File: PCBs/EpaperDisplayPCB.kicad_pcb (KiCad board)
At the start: 2 copper layers, 84 x 40.1 mm, 52 parts, among them J1 Conn_01x12_FPC_0.5mm, J2 Conn_01x08, Q1 AO3404A, U1 ePaper-2.66, U2 LIS3DH

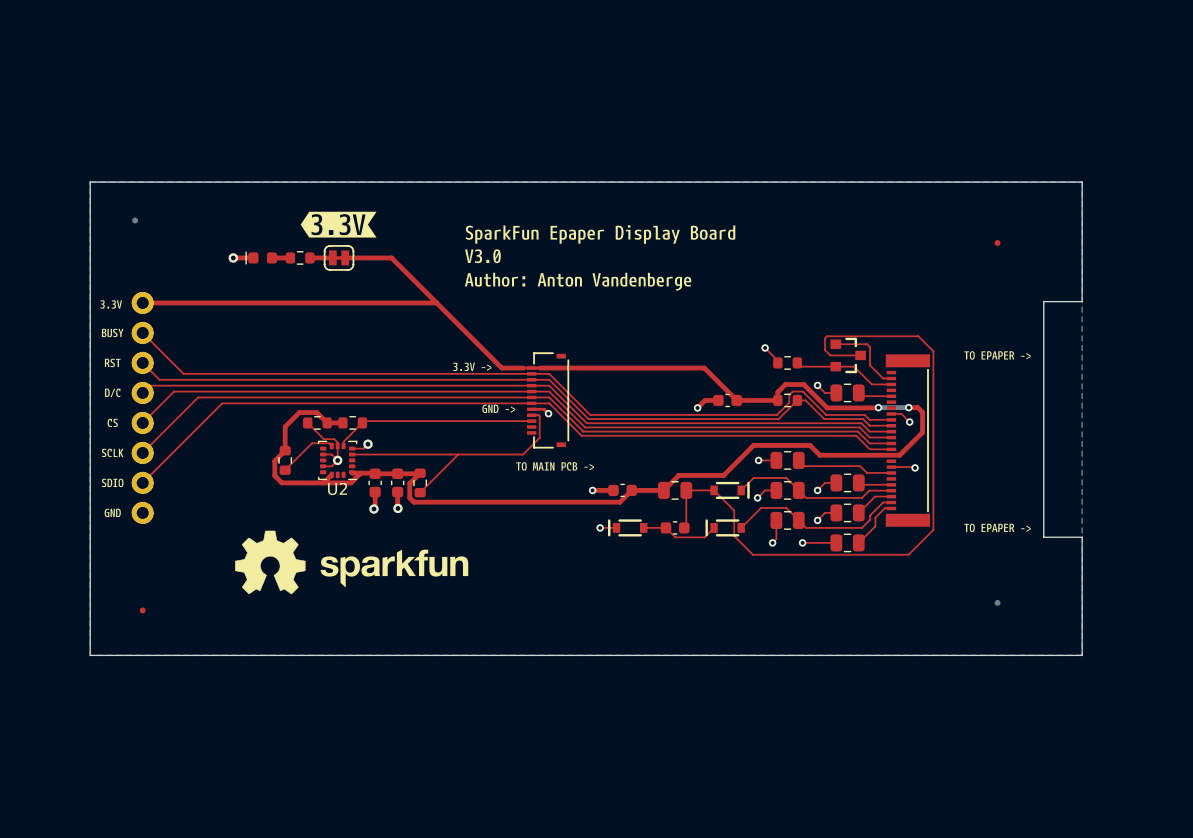
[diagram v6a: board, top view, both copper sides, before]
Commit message: Adding updates From review
Fixed epaper to main board FPC connection.
Added fiducials to main board for stencil alignment purposes.
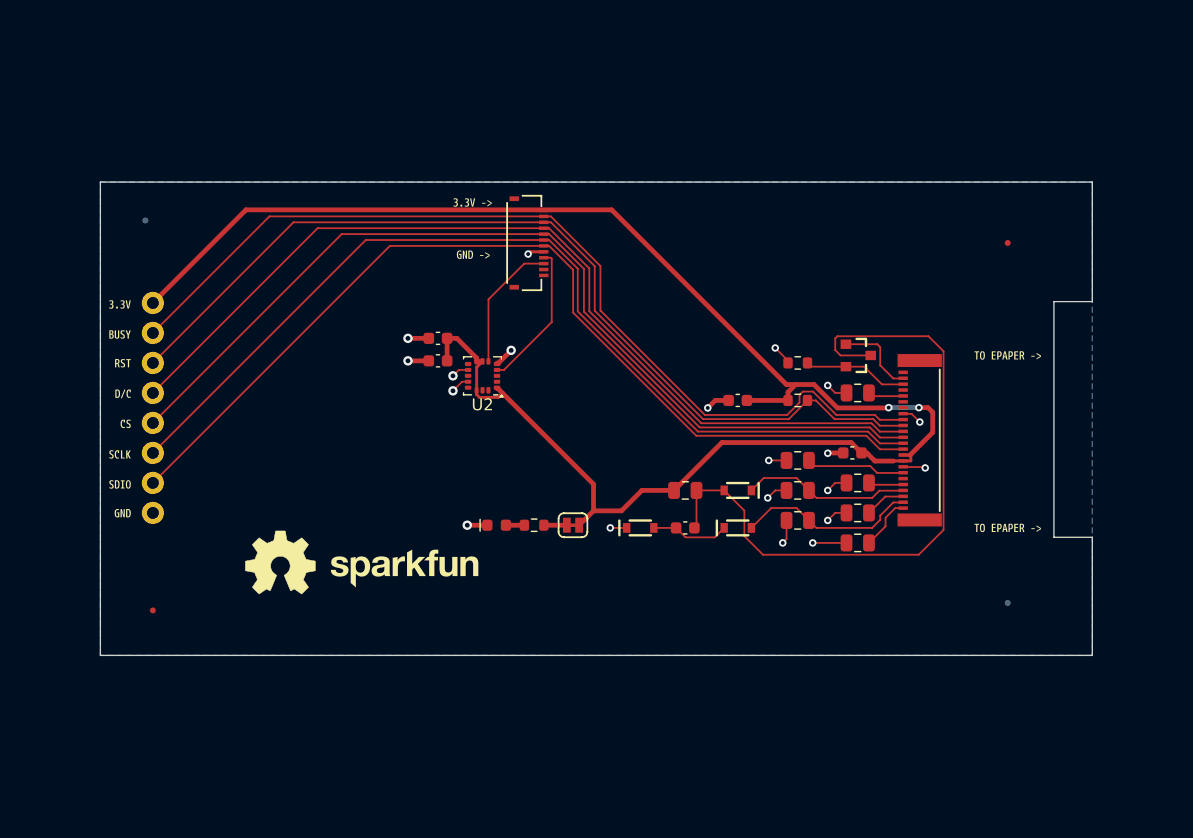
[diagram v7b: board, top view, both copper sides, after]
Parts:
- removed R4, R7: 10k, SparkFun-Resistor:R_0603_1608Metric
- removed R5, R6: 4.7k, SparkFun-Resistor:R_0603_1608Metric
- removed kibuzzard-65E13155: G***, kibuzzard-65E13155
- removed kibuzzard-65ECA227: G***, kibuzzard-65ECA227
- removed kibuzzard-65EF974B: G***, kibuzzard-65EF974B
- moved D4 30.1 mm to (152.8, 96.8)
- moved JP1 30.1 mm to (159.2, 96.8)
- moved R3 30.1 mm to (155.9, 96.8)
- moved C2 19.7 mm to (182.9, 90.7)
- moved U2 14.2 mm to (151.6, 84.2)
- moved kibuzzard-65E131D6 13.9 mm to (150.7, 69.5)
- moved J1 13.4 mm to (155.4, 72.9), turned to -90 degrees
- moved kibuzzard-65E131AD 13.2 mm to (150.8, 73.9)
- moved C12 12.7 mm to (147.8, 81.0), turned to 180 degrees
- moved C11 11.6 mm to (147.8, 82.9), turned to 180 degrees
- moved kibuzzard-65B20040 1.10 mm to (121.4, 88.3)
- moved U1 1.00 mm to (201.6, 87.6)
- moved kibuzzard-65B20037 0.88 mm to (121.1, 85.7)
- moved kibuzzard-65B20022 0.87 mm to (121.1, 83.1)
- moved C10 0.86 mm to (183.4, 98.3)
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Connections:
- J1 pad 1: unconnected-(J1-Pin_1-Pad1) -> +3.3V
- J1 pad 10: ~{RST} -> SDA
- J1 pad 11: ~{BUSY} -> unconnected-(J1-Pin_11-Pad11)
- J1 pad 12: +3.3V -> unconnected-(J1-Pin_12-Pad12)
- J1 pad 2: unconnected-(J1-Pin_2-Pad2) -> ~{BUSY}
- J1 pad 3: SDA -> ~{RST}
- J1 pad 4: SCL -> D/~{C}
- J1 pad 5: GND -> ~{CS}
- J1 pad 6: SDIO -> SCLK
- J1 pad 7: SCLK -> SDIO
- J1 pad 8: ~{CS} -> GND
- J1 pad 9: D/~{C} -> SCL
- U2 pad 7: GND -> +3.3V
- U2 pad 8: Net-(U2-CS) -> +3.3V
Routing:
- net D/~{C}: track 65.3 -> 78.4 mm
- net SDIO: track 68.0 -> 81.2 mm
- net SCLK: track 67.0 -> 80.1 mm
- net ~{CS}: track 66.1 -> 79.3 mm
- net +3.3V: track 156.5 -> 143.7 mm
- net ~{RST}: track 66.9 -> 79.0 mm
- net SCL: track 23.6 -> 12.4 mm
- net ~{BUSY}: track 68.5 -> 78.9 mm
- net SDA: track 17.0 -> 11.2 mm
- net Net-(U2-CS): track 4.98 -> 0.00 mm
- net GND: track 39.8 -> 35.5 mm, vias 19 -> 20
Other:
- outline, holes or cut-outs redrawn

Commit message: Adding Fiducials to Epaper
Adding stencil alignment fiducials to epaper PCB
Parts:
- added FID10: Fiducial_3mm, SparkFun-Aesthetic:Fiducial_1.5mm_Mask3mm, F.Cu at (208.2, 67.9)
- added FID11: Fiducial_3mm, SparkFun-Aesthetic:Fiducial_1.5mm_Mask3mm, F.Cu at (114.2, 87.9)
- added FID12: Fiducial_3mm, SparkFun-Aesthetic:Fiducial_1.5mm_Mask3mm, F.Cu at (114.2, 67.9)
- added FID13: Fiducial_3mm, SparkFun-Aesthetic:Fiducial_1.5mm_Mask3mm, F.Cu at (131.2, 55.9)
- added FID14: Fiducial_3mm, SparkFun-Aesthetic:Fiducial_1.5mm_Mask3mm, F.Cu at (161.2, 55.9)
- added FID15: Fiducial_3mm, SparkFun-Aesthetic:Fiducial_1.5mm_Mask3mm, F.Cu at (191.2, 55.9)
- added FID5: Fiducial_3mm, SparkFun-Aesthetic:Fiducial_1.5mm_Mask3mm, F.Cu at (114.2, 107.9)
- added FID6: Fiducial_3mm, SparkFun-Aesthetic:Fiducial_1.5mm_Mask3mm, F.Cu at (131.2, 119.9)
- added FID7: Fiducial_3mm, SparkFun-Aesthetic:Fiducial_1.5mm_Mask3mm, F.Cu at (161.2, 119.9)
- added FID8: Fiducial_3mm, SparkFun-Aesthetic:Fiducial_1.5mm_Mask3mm, F.Cu at (191.2, 119.9)
- added FID9: Fiducial_3mm, SparkFun-Aesthetic:Fiducial_1.5mm_Mask3mm, F.Cu at (208.2, 107.9)
